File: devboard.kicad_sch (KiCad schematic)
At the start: 28 parts, among them J1 USB4105-GF-A, J2 Conn_01x08_Pin, J3 Conn_01x08_Pin, U1 STM32F411CEU6, U2 AP2120N-3.3TRG1, U3 USBLC6-2SC6Y

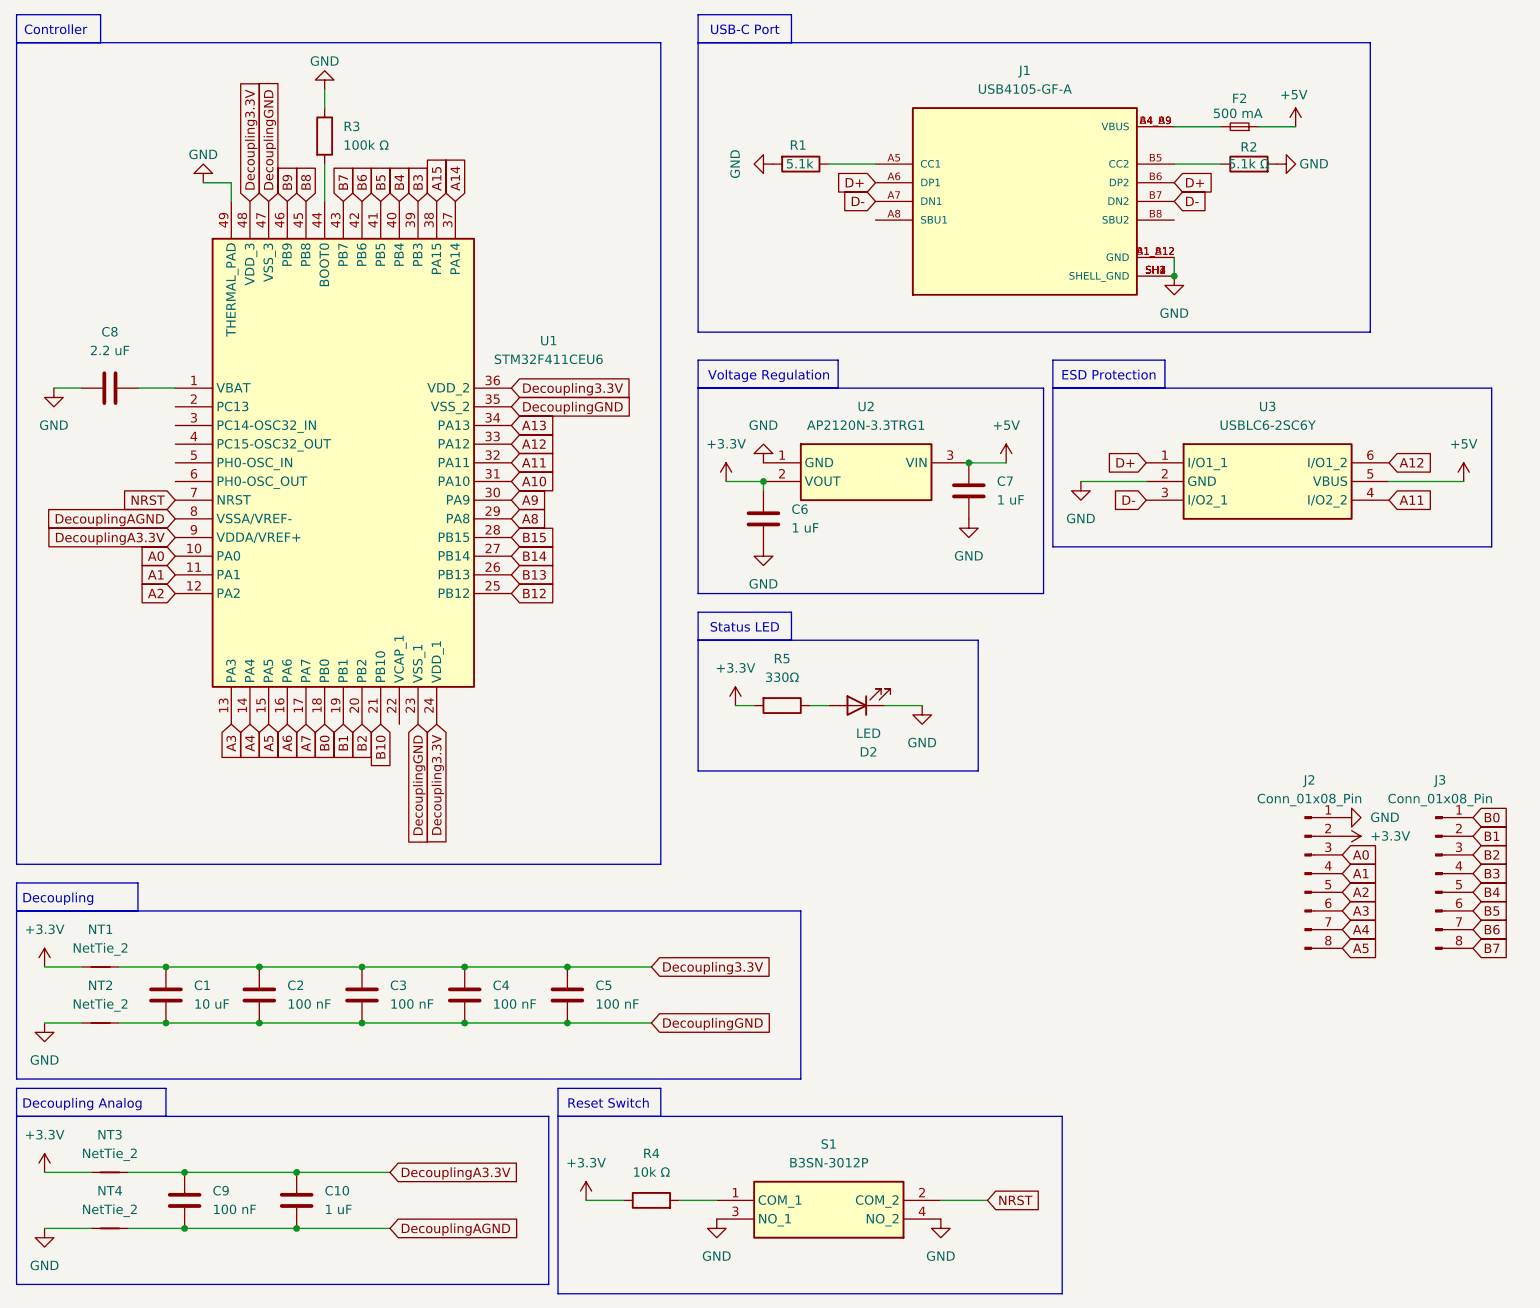
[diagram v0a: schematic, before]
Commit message: Total board refactoring: - Full board routing - Ready for manufacturing - Schematic fixing ad improvements
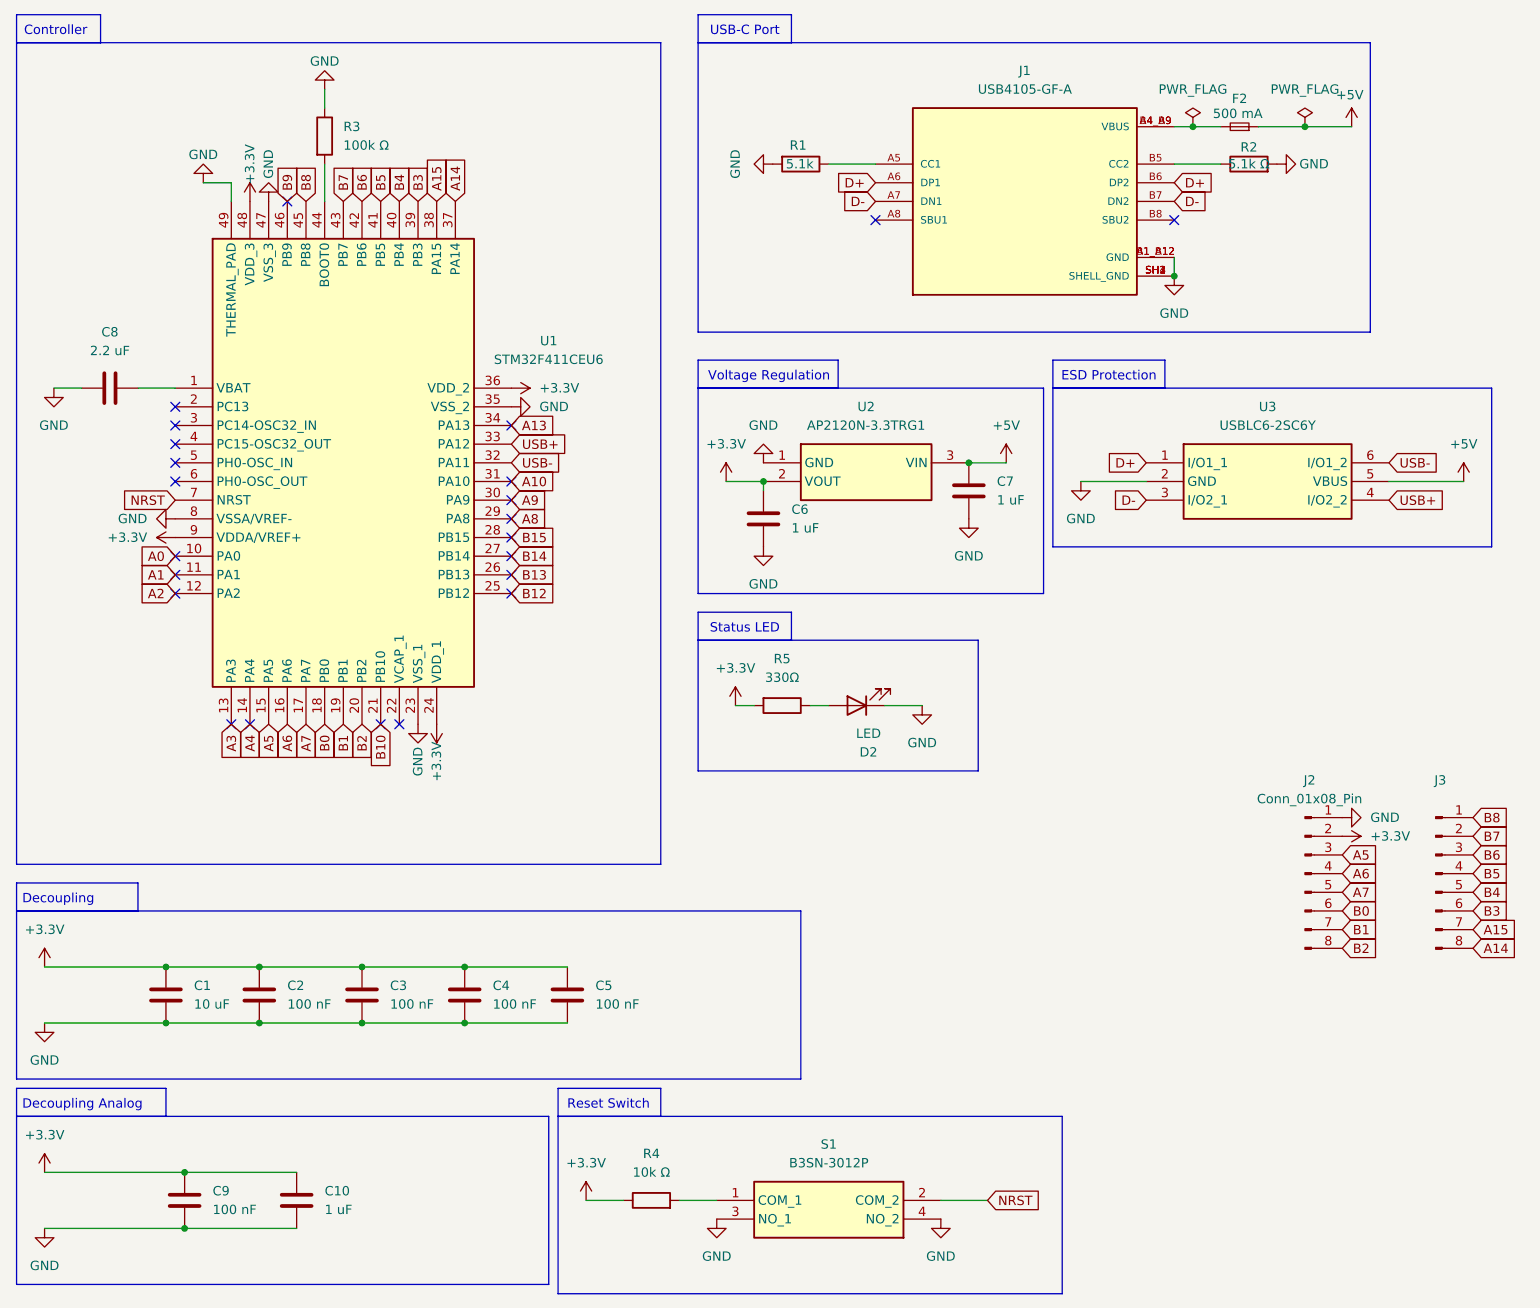
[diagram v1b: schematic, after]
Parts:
- removed NT1, NT2, NT3, NT4: NetTie_2, NetTie:NetTie-2_SMD_Pad0.5mm, symbol Device:NetTie_2
- C1, C10, C2, C3, C4, C5, C9: footprint Capacitor_SMD:C_0603_1608Metric -> Capacitor_SMD:C_0402_1005Metric
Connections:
- net Decoupling3.3V is gone; now on net +3.3V: C1.1, C2.1, C3.1, C4.1, C5.1, U1.24 (VDD_1), U1.36 (VDD_2), U1.48 (VDD_3)
- net DecouplingA3.3V is gone; now on net +3.3V: C10.1, C9.1, U1.9 (VDDA/VREF+)
- net DecouplingAGND is gone; now on net GND: C10.2, C9.2, U1.8 (VSSA/VREF-)
- net DecouplingGND is gone; now on net GND: C1.2, C2.2, C3.2, C4.2, C5.2, U1.23 (VSS_1), U1.35 (VSS_2), U1.47 (VSS_3)
- net A0: no longer J2.3 (Pin_3)
- net A1: no longer J2.4 (Pin_4)
- net A14: now also J3.8 (Pin_8)
- net A15: now also J3.7 (Pin_7)
- net A2: no longer J2.5 (Pin_5)
- net A3: no longer J2.6 (Pin_6)
- net A4: no longer J2.7 (Pin_7)
- net A5: now also J2.3 (Pin_3); no longer J2.8 (Pin_8)
- net A6: now also J2.4 (Pin_4)
- net A7: now also J2.5 (Pin_5)
- net B0: now also J2.6 (Pin_6); no longer J3.1 (Pin_1)
- net B1: now also J2.7 (Pin_7); no longer J3.2 (Pin_2)
- net B2: now also J2.8 (Pin_8); no longer J3.3 (Pin_3)
- net B3: now also J3.6 (Pin_6); no longer J3.4 (Pin_4)
- net B5: now also J3.4 (Pin_4); no longer J3.6 (Pin_6)
- net B6: now also J3.3 (Pin_3); no longer J3.7 (Pin_7)
- net B7: now also J3.2 (Pin_2); no longer J3.8 (Pin_8)
- net B8: now also J3.1 (Pin_1)
- net A11 renamed USB+
- net USB+: now also U1.33 (PA12); no longer U1.32 (PA11)
- net A12 renamed USB-
- net USB-: now also U1.32 (PA11); no longer U1.33 (PA12)
- no-connect marks 0 -> 23

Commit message: Fix VBAT
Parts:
- C8: value 2.2 uF -> 100 nF
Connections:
- net +3.3V: now also C8.2, U1.1 (VBAT)
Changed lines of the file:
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@@
 	)
 	(junction
+		(at 35.56 69.85)
+		(diameter 0)
+		(color 0 0 0 0)
+	)
+	(junction
 		(at 35.56 148.59)
 		(diameter 0)
@@
 	(wire
 		(pts
+			(xy 35.56 69.85) (xy 36.83 69.85)
+		)
+		(stroke
+			(width 0)
+			(type default)
+		)
+	)
+	(wire
+		(pts
 			(xy 160.02 82.55) (xy 168.91 82.55)
 		)
@@
 	(wire
 		(pts
-			(xy 31.75 69.85) (xy 36.83 69.85)
+			(xy 31.75 69.85) (xy 35.56 69.85)
 		)
 		(stroke
@@
 	)
 	(symbol
+		(lib_id "power:+3.3V")
+		(at 35.56 69.85 0)
+		(unit 1)
+		(exclude_from_sim no)
+		(in_bom yes)
+		(on_board yes)
+		(dnp no)
+		(fields_autoplaced yes)
+		(property "Reference" "#PWR034"
+			(at 35.56 73.66 0)
+			(effects
+				(font
+					(size 1.27 1.27)
+				)
+				(hide yes)
+			)
+		)
+		(property "Value" "+3.3V"
+			(at 35.56 64.77 0)
+			(effects
+				(font
+					(size 1.27 1.27)
+				)
+			)
+		)
+		(property "Footprint" ""
+			(at 35.56 69.85 0)
+			(effects
+				(font
+					(size 1.27 1.27)
+				)
+				(hide yes)
+			)
+		)
+		(property "Datasheet" ""
+			(at 35.56 69.85 0)
+			(effects
+				(font
+					(size 1.27 1.27)
+				)
+				(hide yes)
+			)
+		)
+		(property "Description" "Power symbol creates a global label with name \"+3.3V\""
+			(at 35.56 69.85 0)
+			(effects
+				(font
+					(size 1.27 1.27)
+				)
+				(hide yes)
+			)
+		)
+		(pin "1"
+		)
+		(instances
+			(project ""
+				(path "/a4930b62-acd9-49da-a994-ca1f96906077"
+					(reference "#PWR034")
+					(unit 1)
+				)
+			)
+		)
+	)
+	(symbol
 		(lib_id "USB4105-GF-A:USB4105-GF-A")
 		(at 152.4 44.45 0)
@@
 			)
 		)
-		(property "Value" "2.2 uF"
+		(property "Value" "100 nF"
 			(at 27.94 64.77 90)
 			(effects

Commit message: Fixes
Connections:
- net D+: now also U3.3 (I/O2_1); no longer U3.1 (I/O1_1)
- net D-: now also U3.1 (I/O1_1); no longer U3.3 (I/O2_1)

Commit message: Increase PWR LED resistence value + better silkscreen placement
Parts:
- R5: value 330Ω -> 10k Ω
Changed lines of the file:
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@@
 			)
 		)
-		(property "Value" "330Ω"
+		(property "Value" "10k Ω"
 			(at 119.38 109.22 90)
 			(effects

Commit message: Expose A13 to work with ST-Link
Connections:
- net A13: now also J3.8 (Pin_8)
- net A14: now also J3.7 (Pin_7); no longer J3.8 (Pin_8)
- net A15: now also J3.6 (Pin_6); no longer J3.7 (Pin_7)
- net B3: now also J3.5 (Pin_5); no longer J3.6 (Pin_6)
- net B4: now also J3.4 (Pin_4); no longer J3.5 (Pin_5)
- net B5: now also J3.3 (Pin_3); no longer J3.4 (Pin_4)
- net B6: now also J3.2 (Pin_2); no longer J3.3 (Pin_3)
- net B7: now also J3.1 (Pin_1); no longer J3.2 (Pin_2)
- net B8: no longer J3.1 (Pin_1)
